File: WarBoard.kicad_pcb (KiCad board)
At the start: 2 copper layers, 114 x 98 mm, 46 parts, among them J1 OLED_128x64, SW1 RotaryEncoder_Switch, SW2 RotaryEncoder_Switch, SW3 Reset, SW4 SW_SPDT_321, U1 WS2812B-4020, U10 DRV2505L, U3 SuperMini nRF52840, U4 WS2812B-4020, U5 WS2812B-4020, U6 WS2812B-4020, U7 SKRHAAE010, U8 JoyStick, U9 MPU6050

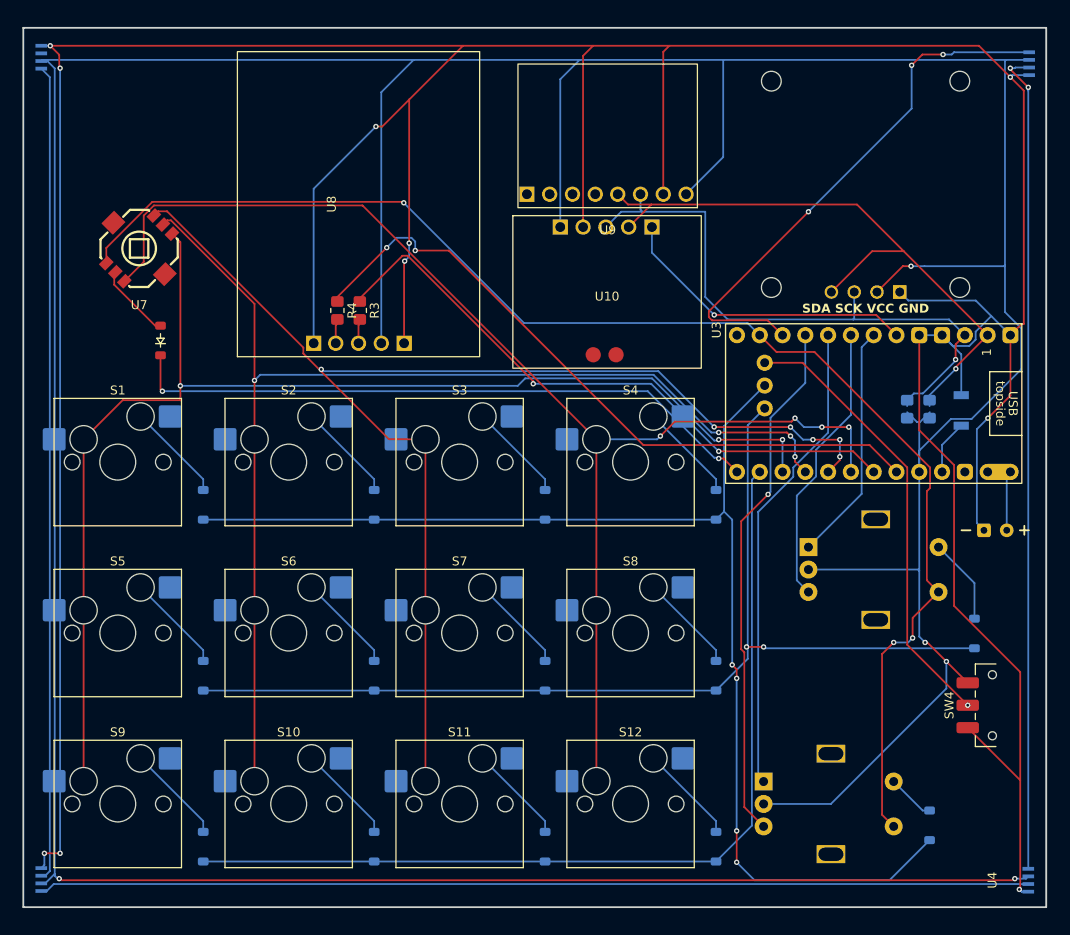
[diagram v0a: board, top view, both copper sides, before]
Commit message: routing-experiment: battery wiring and net class fixes
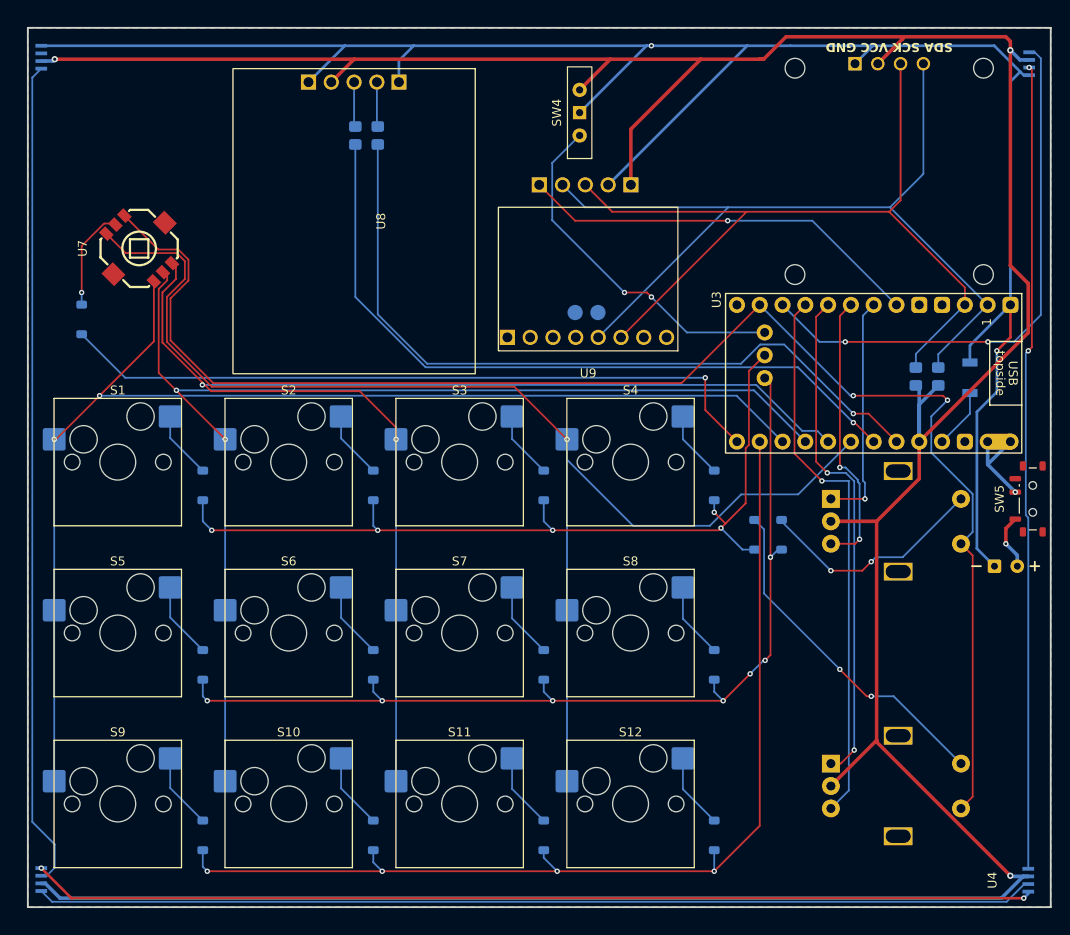
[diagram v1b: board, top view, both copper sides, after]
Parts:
- added SW5: Switch, Button_Switch_SMD:SW_SPDT_Shouhan_MSK12C02, F.Cu at (-502.9, -0.64)
- D20, R3, R4, U10: moved to B.Cu
- SW4: footprint Button_Switch_SMD:SW_SPDT_CK_JS102011SAQN -> Button_Switch_THT:SW_Slide-03_Wuerth-WS-SLTV_10x2.5x6.4_P2.54mm
- moved SW4 80.5 mm to (-553.4, -43.7)
- moved U8 41.6 mm to (-565.0, -48.6), turned to -90 degrees
- moved D18 37.8 mm to (-533.9, 3.36)
- moved D19 24.2 mm to (-530.9, 3.36)
- moved R4 20.0 mm to (-575.9, -41.1), turned to 90 degrees
- moved R3 19.5 mm to (-578.4, -41.1), turned to 90 degrees
- moved U10 19.0 mm to (-542.4, -36.9), turned to 180 degrees
- moved U9 16.1 mm to (-542.4, -17.1)
- moved D20 9.09 mm to (-608.9, -20.6)
- moved SW1 7.76 mm to (-517.9, 31.4)
- moved SW2 5.93 mm to (-517.9, 1.86)
- moved BT1 4.17 mm to (-505.9, 6.86)
- moved SW3 3.77 mm to (-509.9, -14.1)
- moved R1 3.77 mm to (-515.9, -14.3)
- moved R2 3.77 mm to (-513.4, -14.3)
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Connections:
- BT1 pad 2: GND -> Net-(BT1--)
- U3 pad 13: unconnected-(U3-BAT+-Pad13) -> Net-(SW5-Pad2)
- U3 pad 14: unconnected-(U3-GND-Pad14) -> Net-(BT1--)
- U3 pad 29: Net-(BT1-+) -> Net-(SW5-Pad2)
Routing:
- net GND: track 473.0 -> 335.2 mm, vias 10 -> 4
- net VCC: track 526.3 -> 388.8 mm, vias 5 -> 3
- net Row_0: track 138.2 -> 97.1 mm, vias 4 -> 5
- net Net-(D18-A): track 5.34 -> 38.4 mm, vias 0 -> 2
- net SDA: track 71.8 -> 100.2 mm, vias 1 -> 0
- net SCL: track 68.3 -> 95.0 mm, vias 1 -> 0
- net Net-(D19-A): track 9.63 -> 25.7 mm, vias 0 -> 2
- net Row_2: track 102.6 -> 117.1 mm, vias 0 -> 4
- net Col_4: track 152.7 -> 165.4 mm, vias 3 -> 2
- net JX: track 69.4 -> 81.4 mm, vias 2 -> 1
- net HAP_TRIG: track 33.9 -> 45.4 mm
- net Net-(SW5-Pad2): track 0.00 -> 10.5 mm, vias 0 -> 1
- net LAY: track 50.0 -> 39.6 mm, vias 1 -> 2
- net Row_3: track 71.9 -> 80.1 mm, vias 2 -> 1
- net JY: track 76.4 -> 84.4 mm, vias 2 -> 1
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- added copper zone on B.Cu, net GND
- added copper zone on F.Cu, net VCC

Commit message: Final Iter
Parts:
- SW5: moved to B.Cu
- moved SW5 2.00 mm to (-504.9, -0.64), turned to -90 degrees
- moved BT1 1.50 mm to (-505.9, 8.36)
- moved U1 1.32 mm to (-504.4, -49.9)
- moved U5 1.06 mm to (-612.4, 42.1)
- moved U4 1.00 mm to (-504.4, 41.9)
- moved U6 1.00 mm to (-612.4, -49.9)
- moved D18 0.50 mm to (-534.4, 3.36)
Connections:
- SW5 pad 1: Net-(BT1-+) -> Net-(SW5-Pad1)
- SW5 pad 2: Net-(SW5-Pad2) -> Net-(BT1-+)
- U3 pad 12: unconnected-(U3-P1.06-LF-Pad12) -> JS
- U3 pad 13: Net-(SW5-Pad2) -> Net-(SW5-Pad1)
- U3 pad 29: Net-(SW5-Pad2) -> Net-(SW5-Pad1)
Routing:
- net JS: track 0.00 -> 63.7 mm, vias 0 -> 2
- net GND: track 335.2 -> 308.2 mm, vias 4 -> 15
- net VCC: track 388.8 -> 412.6 mm, vias 3 -> 15
- net Col_2: track 151.6 -> 128.9 mm, vias 2 -> 4
- net Net-(BT1--): track 0.00 -> 22.1 mm, vias 0 -> 1
- net Col_3: track 147.9 -> 164.2 mm, vias 1 -> 5
- net Net-(D18-A): track 38.4 -> 51.6 mm
- net Net-(SW5-Pad2): track 10.5 -> 0.00 mm, vias 1 -> 0
- net Col_0: track 138.7 -> 147.3 mm
- net Net-(BT1-+): track 6.21 -> 13.5 mm, vias 1 -> 2
- net JX: track 81.4 -> 88.7 mm, vias 1 -> 2
- net Net-(D19-A): track 25.7 -> 32.3 mm, vias 2 -> 5
- net HAP_TRIG: track 45.4 -> 51.2 mm
- net Net-(SW5-Pad1): track 0.00 -> 5.38 mm
- net Col_1: track 132.9 -> 138.2 mm, vias 2 -> 4
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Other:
- board size 114 x 98 mm -> 113 x 98 mm

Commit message: fix vcc plane mapping
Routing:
- net VCC: track 412.6 -> 0.31 mm, vias 15 -> 6

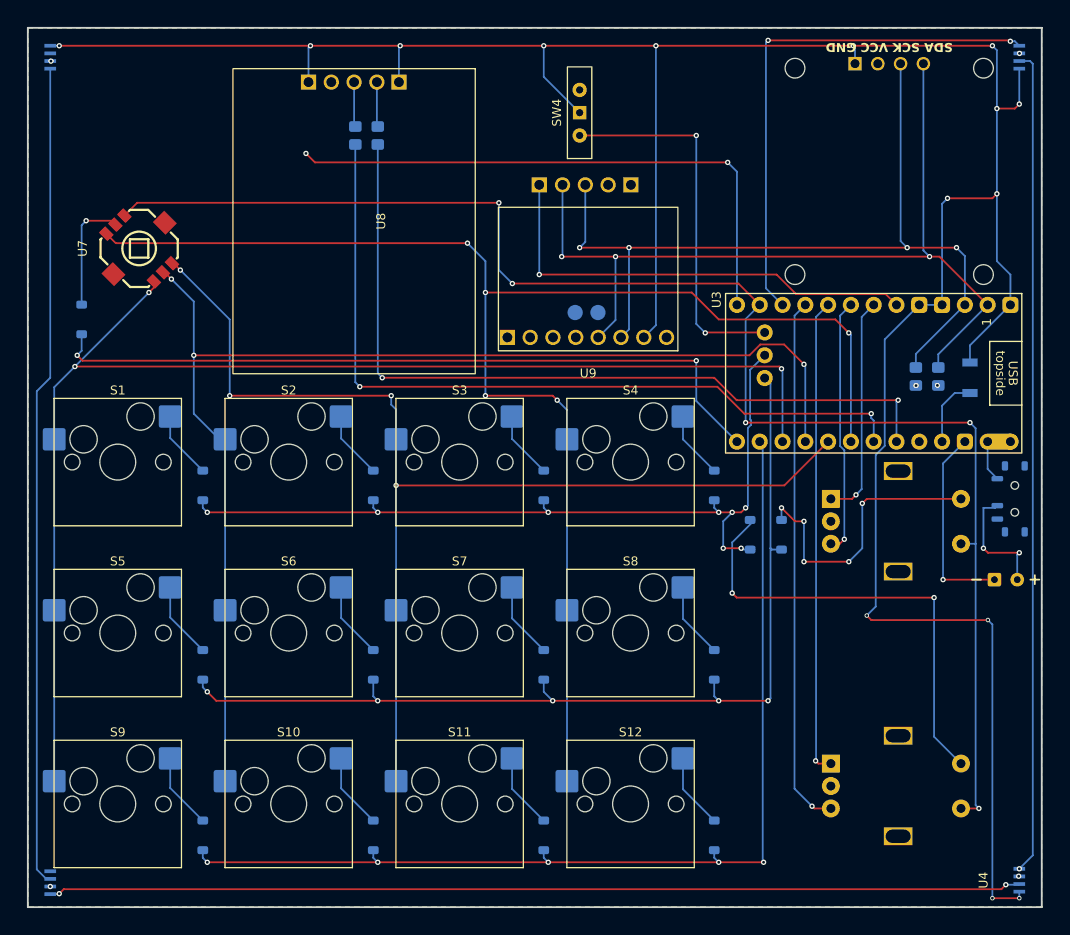
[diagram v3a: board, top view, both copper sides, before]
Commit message: Mount Points added
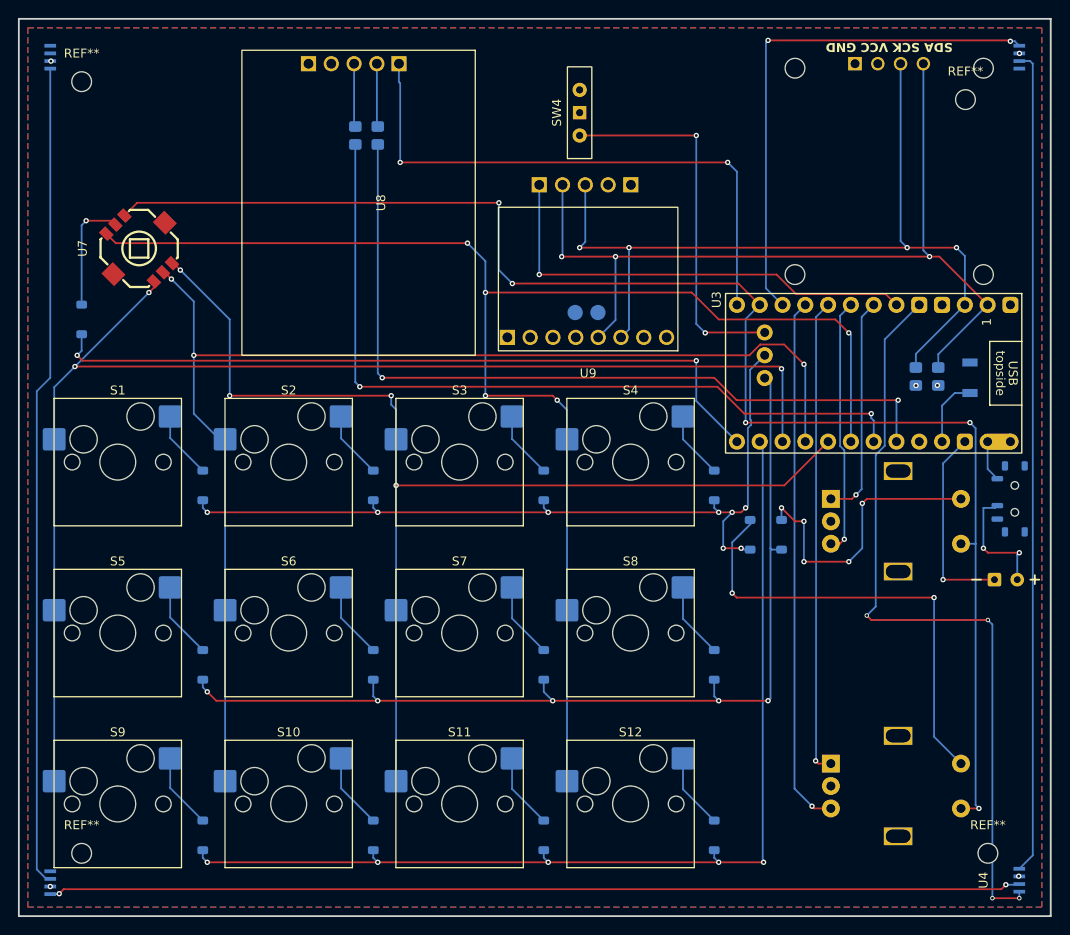
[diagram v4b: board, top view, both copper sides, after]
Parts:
- added REF**: MountingHole_2.2mm_M2, MountingHole:MountingHole_2.2mm_M2, F.Cu at (-507.9, 38.9)
- added REF**: MountingHole_2.2mm_M2, MountingHole:MountingHole_2.2mm_M2, F.Cu at (-510.4, -45.1)
- added REF**: MountingHole_2.2mm_M2, MountingHole:MountingHole_2.2mm_M2, F.Cu at (-608.9, -47.1)
- added REF**: MountingHole_2.2mm_M2, MountingHole:MountingHole_2.2mm_M2, F.Cu at (-608.9, 38.9)
- moved U8 2.05 mm to (-565.0, -50.6)
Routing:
- net GND: track 308.2 -> 85.7 mm, vias 15 -> 4
- net Net-(U8-Y): track 4.99 -> 6.90 mm
- net Net-(U8-X): track 5.00 -> 6.86 mm
- net Col_1: track 138.2 -> 137.4 mm, vias 4 -> 3
- net Net-(SW5-Pad1): track 5.38 -> 4.58 mm
- net Net-(U1-DOUT): vias 1 -> 0
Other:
- board size 113 x 98 mm -> 115 x 100 mm
